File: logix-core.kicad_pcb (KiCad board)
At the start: 6 copper layers, 14 parts, among them U1 XC7A15T-FTG256

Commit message: stuff
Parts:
- added C14: 0.47u, Capacitor_SMD:C_0603_1608Metric, F.Cu at (237.7, 76.0)
- added C15: 10n, Capacitor_SMD:C_0603_1608Metric, F.Cu at (237.7, 78.5)
- added J1: QSH-030-01-X-D-A-XX, QSH-030-01-L-D-A-K:SAMTEC_QSH-030-01-X-D-A-XX, F.Cu at (222.2, 67.3)
- added J2: QSH-030-01-X-D-A-XX, QSH-030-01-L-D-A-K:SAMTEC_QSH-030-01-X-D-A-XX, F.Cu at (222.2, 79.5)
- added J3: 878321420, 878321420:CONN_87832-1420_MOL, F.Cu at (221.0, 91.3)
- added U2: MP5470GL-0000-P, MP5470:QFN-3x4_MP5470_MNP, F.Cu at (234.8, 90.1)
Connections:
- U1 pad F8: unconnected-(U1D-VCCBATT_0-PadF8) -> VCCAUX
- U1 pad G7: unconnected-(U1D-GNDADC_0-PadG7) -> AGND
- U1 pad G8: unconnected-(U1D-VCCADC_0-PadG8) -> VCCAUX
- U1 pad L7: unconnected-(U1C-TCK_0-PadL7) -> /FPGA/FPGA pg.3/JTAG.TCK
- U1 pad M7: unconnected-(U1C-TMS_0-PadM7) -> /FPGA/FPGA pg.3/JTAG.TMS
- U1 pad N7: unconnected-(U1C-TDI_0-PadN7) -> /FPGA/FPGA pg.3/JTAG.TDI
- U1 pad N8: unconnected-(U1C-TDO_0-PadN8) -> /FPGA/FPGA pg.3/JTAG.TDO
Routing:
- net VCCAUX: track 2.83 -> 4.24 mm, vias 4 -> 6
- net unconnected-(U1D-VCCBATT_0-PadF8): track 0.71 -> 0.00 mm, vias 1 -> 0
- net unconnected-(U1D-VCCADC_0-PadG8): track 0.71 -> 0.00 mm, vias 1 -> 0
- net unconnected-(U1D-GNDADC_0-PadG7): track 0.71 -> 0.00 mm, vias 1 -> 0
- net unconnected-(U1C-TMS_0-PadM7): track 0.71 -> 0.00 mm, vias 1 -> 0
- net unconnected-(U1C-TDO_0-PadN8): track 0.71 -> 0.00 mm, vias 1 -> 0
- net unconnected-(U1C-TDI_0-PadN7): track 0.71 -> 0.00 mm, vias 1 -> 0
- net unconnected-(U1C-TCK_0-PadL7): track 0.71 -> 0.00 mm, vias 1 -> 0
- net AGND: track 0.00 -> 0.71 mm, vias 0 -> 1
- net /FPGA/FPGA pg.3/JTAG.TMS: track 0.00 -> 0.71 mm, vias 0 -> 1
- net /FPGA/FPGA pg.3/JTAG.TDO: track 0.00 -> 0.71 mm, vias 0 -> 1
- net /FPGA/FPGA pg.3/JTAG.TDI: track 0.00 -> 0.71 mm, vias 0 -> 1
- net /FPGA/FPGA pg.3/JTAG.TCK: track 0.00 -> 0.71 mm, vias 0 -> 1

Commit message: more stuff!
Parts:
- added C16: 22u, Capacitor_SMD:C_0603_1608Metric, F.Cu at (188.0, 48.2)
- added C17: 22u, Capacitor_SMD:C_0603_1608Metric, F.Cu at (188.0, 50.7)
- added C18: 1u, Capacitor_SMD:C_0402_1005Metric, F.Cu at (187.4, 65.0)
- added C19: 22u, Capacitor_SMD:C_0603_1608Metric, F.Cu at (188.0, 53.2)
- added C20: 22u, Capacitor_SMD:C_0603_1608Metric, F.Cu at (188.0, 55.7)
- added C21: 22u, Capacitor_SMD:C_0603_1608Metric, F.Cu at (188.0, 58.2)
- added C22: 22u, Capacitor_SMD:C_0603_1608Metric, F.Cu at (188.0, 60.8)
- added C23: 47p, Capacitor_SMD:C_0402_1005Metric, F.Cu at (207.1, 90.8)
- added C24: 47p, Capacitor_SMD:C_0402_1005Metric, F.Cu at (207.1, 92.8)
- added C25: 10n, Capacitor_SMD:C_0402_1005Metric, F.Cu at (207.1, 94.7)
- added C26: 100n, Capacitor_SMD:C_0402_1005Metric, F.Cu at (207.1, 96.7)
- added C27: 100n, Capacitor_SMD:C_0402_1005Metric, F.Cu at (207.1, 98.7)
- added C28: 100n, Capacitor_SMD:C_0402_1005Metric, F.Cu at (207.1, 100.6)
- added D1: LED, LED_SMD:LED_0603_1608Metric, F.Cu at (207.7, 102.9)
- added D2: LED, LED_SMD:LED_0603_1608Metric, F.Cu at (207.7, 105.5)
- added FB1: FerriteBead, Resistor_SMD:R_0402_1005Metric_Pad0.72x0.64mm_HandSolder, F.Cu at (199.7, 97.8)
- added L1: 2.2u, Inductor_SMD:L_Bourns-SRN4018, F.Cu at (182.9, 49.7)
- added L2: 2.2u, Inductor_SMD:L_Bourns-SRN4018, F.Cu at (182.9, 55.3)
- added L3: 2.2u, Inductor_SMD:L_Bourns-SRN4018, F.Cu at (182.9, 60.8)
- added L4: 2.2u, Inductor_SMD:L_Bourns-SRN4018, F.Cu at (182.9, 66.4)
- added R1: 10k, Resistor_SMD:R_0402_1005Metric, F.Cu at (187.4, 63.0)
- added R10: 100, Resistor_SMD:R_0402_1005Metric_Pad0.72x0.64mm_HandSolder, F.Cu at (204.0, 106.7)
- added R2: 27.4, Resistor_SMD:R_0402_1005Metric_Pad0.72x0.64mm_HandSolder, F.Cu at (204.0, 90.8)
- added R3: 27.4, Resistor_SMD:R_0402_1005Metric_Pad0.72x0.64mm_HandSolder, F.Cu at (204.0, 92.8)
- added R4: 0, Resistor_SMD:R_0402_1005Metric_Pad0.72x0.64mm_HandSolder, F.Cu at (204.0, 94.8)
- added R5: 0, Resistor_SMD:R_0402_1005Metric_Pad0.72x0.64mm_HandSolder, F.Cu at (204.0, 96.8)
- added R6: 0, Resistor_SMD:R_0402_1005Metric_Pad0.72x0.64mm_HandSolder, F.Cu at (204.0, 98.8)
- added R7: 0, Resistor_SMD:R_0402_1005Metric_Pad0.72x0.64mm_HandSolder, F.Cu at (204.0, 100.7)
- added R8: 100, Resistor_SMD:R_0402_1005Metric_Pad0.72x0.64mm_HandSolder, F.Cu at (204.0, 102.7)
- added R9: 100, Resistor_SMD:R_0402_1005Metric_Pad0.72x0.64mm_HandSolder, F.Cu at (204.0, 104.7)
- added U3: TPUSBLC6-4SC6, Package_TO_SOT_SMD:SOT-23-6_Handsoldering, F.Cu at (195.1, 99.1)
- added U4: FT230XQ, Package_DFN_QFN:QFN-16-1EP_4x4mm_P0.65mm_EP2.1x2.1mm, F.Cu at (195.3, 93.6)
- added USB1: USB-MR-D-037, USB-MR-D-037:MICRO-USB-SMD_DEALON_USB-MR-D-037, F.Cu at (182.3, 93.2)
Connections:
- U2 pad 1: unconnected-(U2-VIN1-Pad1) -> /PMIC/VIN
- U2 pad 10: unconnected-(U2-FB3-Pad10) -> Net-(U2-FB3)
- U2 pad 13: unconnected-(U2-SW3-Pad13) -> Net-(U2-SW3)
- U2 pad 15: unconnected-(U2-SW4-Pad15) -> Net-(U2-SW4)
- U2 pad 16: unconnected-(U2-VCC-Pad16) -> Net-(U2-VCC)
- U2 pad 18: unconnected-(U2-FB4-Pad18) -> Net-(U2-FB4)
- U2 pad 2: unconnected-(U2-SW1-Pad2) -> Net-(U2-SW1)
- U2 pad 20: unconnected-(U2-GPIO-Pad20) -> Net-(U2-GPIO)
- U2 pad 21: unconnected-(U2-SGND1-Pad21) -> GND
- U2 pad 22: unconnected-(U2-FB1-Pad22) -> Net-(U2-FB1)
- U2 pad 4: unconnected-(U2-SW2-Pad4) -> Net-(U2-SW2)
- U2 pad 5: unconnected-(U2-VIN2-Pad5) -> /PMIC/VIN
- U2 pad 6: unconnected-(U2-FB2-Pad6) -> Net-(U2-FB2)
- U2 pad 9: unconnected-(U2-SGND2-Pad9) -> GND

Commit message: more stuff
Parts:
- added U5: MX25L3233FZN, Package_SON:WSON-8-1EP_6x5mm_P1.27mm_EP3.4x4mm, F.Cu at (202.3, 61.1)

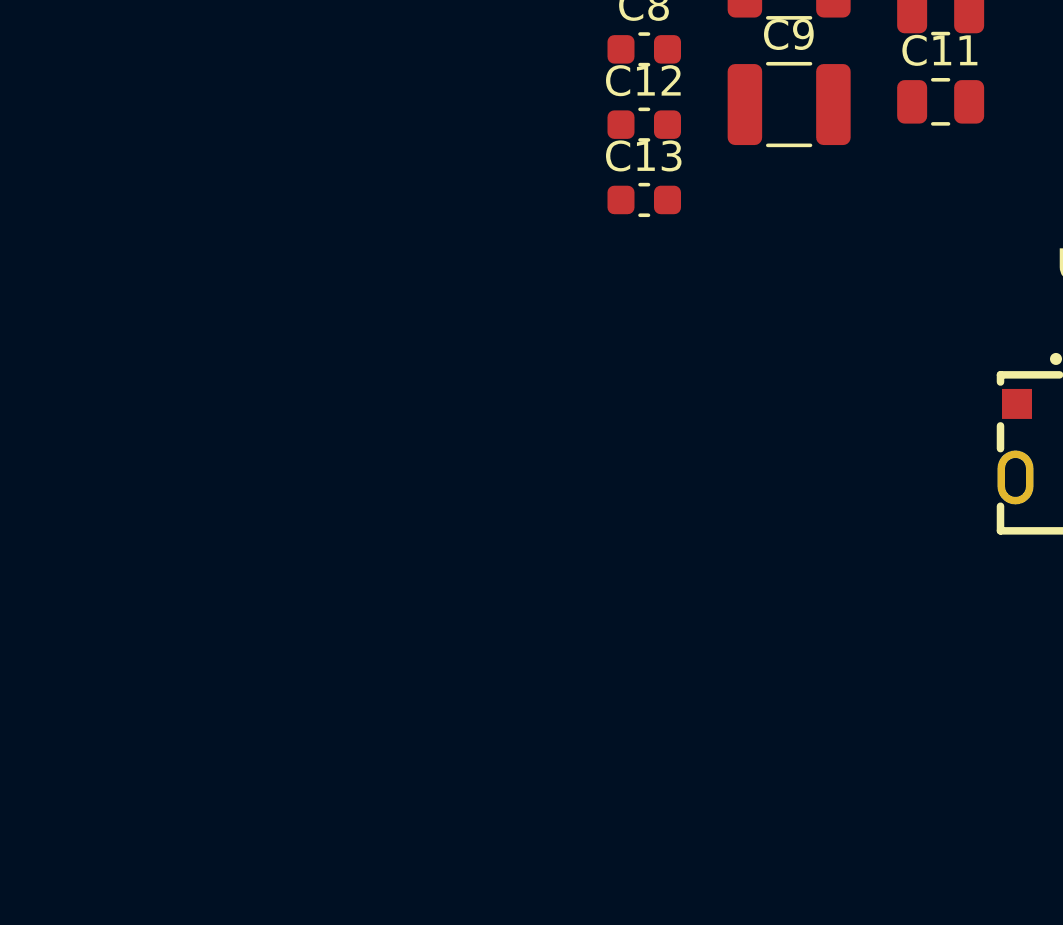
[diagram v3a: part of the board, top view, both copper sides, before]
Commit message: changed ftg256 to csg325, wanted xc7a12t but couldnt find
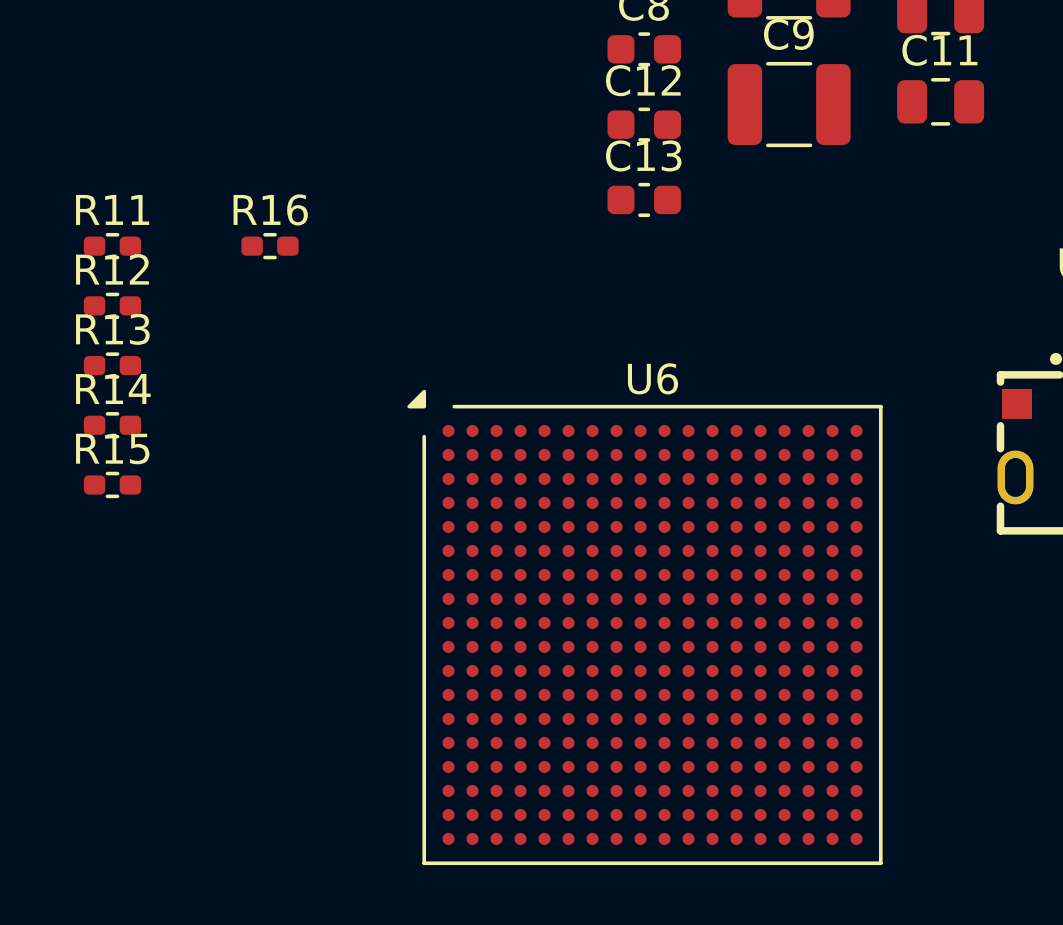
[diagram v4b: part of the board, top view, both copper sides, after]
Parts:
- added R11: 0, Resistor_SMD:R_0402_1005Metric_Pad0.72x0.64mm_HandSolder, F.Cu at (149.0, 87.0)
- added R12: 0, Resistor_SMD:R_0402_1005Metric_Pad0.72x0.64mm_HandSolder, F.Cu at (149.0, 89.0)
- added R13: 0, Resistor_SMD:R_0402_1005Metric_Pad0.72x0.64mm_HandSolder, F.Cu at (149.0, 91.0)
- added R14: 0, Resistor_SMD:R_0402_1005Metric_Pad0.72x0.64mm_HandSolder, F.Cu at (149.0, 93.0)
- added R15: 0, Resistor_SMD:R_0402_1005Metric_Pad0.72x0.64mm_HandSolder, F.Cu at (149.0, 95.0)
- added R16: 0, Resistor_SMD:R_0402_1005Metric_Pad0.72x0.64mm_HandSolder, F.Cu at (154.2, 87.0)
- added U6: XC7A15T-CSG325, Package_BGA:Xilinx_CSG325, F.Cu at (167.0, 100.0)
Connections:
- U1 pad A1: GND -> (no net)
- U1 pad A11: GND -> (no net)
- U1 pad A2: unconnected-(U1B-IO_L8N_T1_AD14N_35-PadA2) -> (no net)
- U1 pad A3: unconnected-(U1B-IO_L4N_T0_35-PadA3) -> (no net)
- U1 pad A4: unconnected-(U1B-IO_L3N_T0_DQS_AD5N_35-PadA4) -> (no net)
- U1 pad A5: unconnected-(U1B-IO_L3P_T0_DQS_AD5P_35-PadA5) -> (no net)
- U1 pad A6: unconnected-(U1B-VCCO_35-PadA6) -> (no net)
- U1 pad A7: unconnected-(U1B-IO_L1N_T0_AD4N_35-PadA7) -> (no net)
- U1 pad B1: unconnected-(U1B-IO_L9N_T1_DQS_AD7N_35-PadB1) -> (no net)
- U1 pad B2: unconnected-(U1B-IO_L8P_T1_AD14P_35-PadB2) -> (no net)
- U1 pad B3: unconnected-(U1B-VCCO_35-PadB3) -> (no net)
- U1 pad B4: unconnected-(U1B-IO_L4P_T0_35-PadB4) -> (no net)
- U1 pad B5: unconnected-(U1B-IO_L2N_T0_AD12N_35-PadB5) -> (no net)
- U1 pad B6: unconnected-(U1B-IO_L2P_T0_AD12P_35-PadB6) -> (no net)
- U1 pad B7: unconnected-(U1B-IO_L1P_T0_AD4P_35-PadB7) -> (no net)
- U1 pad B8: GND -> (no net)
- U1 pad C1: unconnected-(U1B-IO_L9P_T1_DQS_AD7P_35-PadC1) -> (no net)
- U1 pad C15: GND -> (no net)
- U1 pad C2: unconnected-(U1B-IO_L7N_T1_AD6N_35-PadC2) -> (no net)
- U1 pad C3: unconnected-(U1B-IO_L7P_T1_AD6P_35-PadC3) -> (no net)
- U1 pad C4: unconnected-(U1B-IO_L12N_T1_MRCC_35-PadC4) -> (no net)
- U1 pad C5: GND -> (no net)
- U1 pad C6: unconnected-(U1B-IO_L5N_T0_AD13N_35-PadC6) -> (no net)
- U1 pad C7: unconnected-(U1B-IO_L5P_T0_AD13P_35-PadC7) -> (no net)
- U1 pad D1: unconnected-(U1B-IO_L10N_T1_AD15N_35-PadD1) -> (no net)
- U1 pad D12: GND -> (no net)
- U1 pad D2: GND -> (no net)
- U1 pad D3: unconnected-(U1B-IO_L11N_T1_SRCC_35-PadD3) -> (no net)
- U1 pad D4: unconnected-(U1B-IO_L12P_T1_MRCC_35-PadD4) -> (no net)
- U1 pad D5: unconnected-(U1B-IO_L6N_T0_VREF_35-PadD5) -> (no net)
- U1 pad D6: unconnected-(U1B-IO_L6P_T0_35-PadD6) -> (no net)
- U1 pad D7: unconnected-(U1B-VCCO_35-PadD7) -> (no net)
- U1 pad E1: unconnected-(U1B-IO_L15N_T2_DQS_35-PadE1) -> (no net)
- U1 pad E10: VCCBRAM -> (no net)
- U1 pad E2: unconnected-(U1B-IO_L10P_T1_AD15P_35-PadE2) -> (no net)
- U1 pad E3: unconnected-(U1B-IO_L11P_T1_SRCC_35-PadE3) -> (no net)
- U1 pad E4: unconnected-(U1B-VCCO_35-PadE4) -> (no net)
- U1 pad E5: unconnected-(U1B-IO_L13N_T2_MRCC_35-PadE5) -> (no net)
- U1 pad E6: unconnected-(U1B-IO_0_35-PadE6) -> (no net)
- U1 pad E8: unconnected-(U1C-CCLK_0-PadE8) -> /FPGA/FPGA pg.3/INT_FLASH_SPI_CLK
- U1 pad E9: GND -> (no net)
- U1 pad F1: unconnected-(U1B-VCCO_35-PadF1) -> (no net)
- U1 pad F10: GND -> (no net)
- U1 pad F11: VCCBRAM -> (no net)
- U1 pad F16: GND -> (no net)
- U1 pad F2: unconnected-(U1B-IO_L15P_T2_DQS_35-PadF2) -> (no net)
- U1 pad F3: unconnected-(U1B-IO_L14N_T2_SRCC_35-PadF3) -> (no net)
- U1 pad F4: unconnected-(U1B-IO_L14P_T2_SRCC_35-PadF4) -> (no net)
- U1 pad F5: unconnected-(U1B-IO_L13P_T2_MRCC_35-PadF5) -> (no net)
- U1 pad F6: GND -> (no net)
- U1 pad F7: VCCINT -> (no net)
- U1 pad F8: VCCAUX -> (no net)
- U1 pad F9: VCCINT -> (no net)
- U1 pad G1: unconnected-(U1B-IO_L17N_T2_35-PadG1) -> (no net)
- U1 pad G10: VCCAUX -> (no net)
- U1 pad G13: GND -> (no net)
- U1 pad G2: unconnected-(U1B-IO_L17P_T2_35-PadG2) -> (no net)
- U1 pad G3: GND -> (no net)
- U1 pad G4: unconnected-(U1B-IO_L16N_T2_35-PadG4) -> (no net)
- U1 pad G5: unconnected-(U1B-IO_L16P_T2_35-PadG5) -> (no net)
- U1 pad G6: VCCINT -> (no net)
- U1 pad G7: AGND -> (no net)
- U1 pad G8: VCCAUX -> (no net)
- U1 pad G9: GND -> (no net)
- U1 pad H1: unconnected-(U1B-IO_L20N_T3_35-PadH1) -> (no net)
- U1 pad H2: unconnected-(U1B-IO_L20P_T3_35-PadH2) -> (no net)
- U1 pad H3: unconnected-(U1B-IO_L21N_T3_DQS_35-PadH3) -> (no net)
- U1 pad H4: unconnected-(U1B-IO_L18N_T2_35-PadH4) -> (no net)
- U1 pad H5: unconnected-(U1B-IO_L18P_T2_35-PadH5) -> (no net)
- U1 pad H6: GND -> (no net)
- U1 pad H9: VCCINT -> (no net)
- U1 pad J1: unconnected-(U1B-IO_L22N_T3_35-PadJ1) -> (no net)
- U1 pad J10: VCCAUX -> (no net)
- U1 pad J11: GND -> (no net)
- U1 pad J13: unconnected-(U1A-IO_L1P_T0_D00_MOSI_14-PadJ13) -> /FPGA/FPGA pg.1/INT_FLASH_SPI_D0
- U1 pad J14: unconnected-(U1A-IO_L1N_T0_D01_DIN_14-PadJ14) -> /FPGA/FPGA pg.1/INT_FLASH_SPI_D1
- U1 pad J2: unconnected-(U1B-VCCO_35-PadJ2) -> (no net)
- U1 pad J3: unconnected-(U1B-IO_L21P_T3_DQS_35-PadJ3) -> (no net)
- U1 pad J4: unconnected-(U1B-IO_L19N_T3_VREF_35-PadJ4) -> (no net)
- U1 pad J5: unconnected-(U1B-IO_L19P_T3_35-PadJ5) -> (no net)
- U1 pad J6: VCCINT -> (no net)
- U1 pad J9: GND -> (no net)
- U1 pad K1: unconnected-(U1B-IO_L22P_T3_35-PadK1) -> (no net)
- U1 pad K11: VCCAUX -> (no net)
- U1 pad K14: GND -> (no net)
- U1 pad K15: unconnected-(U1A-IO_L2P_T0_D02_14-PadK15) -> /FPGA/FPGA pg.1/INT_FLASH_SPI_D2
- U1 pad K16: unconnected-(U1A-IO_L2N_T0_D03_14-PadK16) -> /FPGA/FPGA pg.1/INT_FLASH_SPI_D3
- U1 pad K2: unconnected-(U1B-IO_L24N_T3_35-PadK2) -> (no net)
- U1 pad K3: unconnected-(U1B-IO_L24P_T3_35-PadK3) -> (no net)
- U1 pad K4: GND -> (no net)
- U1 pad K5: unconnected-(U1B-IO_25_35-PadK5) -> (no net)
- U1 pad K6: GND -> (no net)
- U1 pad K9: VCCINT -> (no net)
- U1 pad L1: GND -> (no net)
- U1 pad L10: VCCAUX -> (no net)
- U1 pad L11: GND -> (no net)
- U1 pad L12: unconnected-(U1A-IO_L6P_T0_FCS_B_14-PadL12) -> /FPGA/FPGA pg.1/INT_FLASH_SPI_CS#
- U1 pad L2: unconnected-(U1B-IO_L23N_T3_35-PadL2) -> (no net)
- U1 pad L3: unconnected-(U1B-IO_L23P_T3_35-PadL3) -> (no net)
- U1 pad L4: unconnected-(U1B-IO_L1P_T0_34-PadL4) -> (no net)
- U1 pad L5: unconnected-(U1B-IO_0_34-PadL5) -> (no net)
- U1 pad L8: VCCINT -> (no net)
- U1 pad M1: unconnected-(U1B-IO_L2N_T0_34-PadM1) -> (no net)
- U1 pad M2: unconnected-(U1B-IO_L2P_T0_34-PadM2) -> (no net)
- U1 pad M3: unconnected-(U1B-VCCO_34-PadM3) -> (no net)
- U1 pad M4: unconnected-(U1B-IO_L1N_T0_34-PadM4) -> (no net)
- U1 pad M5: unconnected-(U1B-IO_L6P_T0_34-PadM5) -> (no net)
- U1 pad M8: GND -> (no net)
- U1 pad N1: unconnected-(U1B-IO_L4P_T0_34-PadN1) -> (no net)
- U1 pad N15: GND -> (no net)
- U1 pad N2: unconnected-(U1B-IO_L3N_T0_DQS_34-PadN2) -> (no net)
- U1 pad N3: unconnected-(U1B-IO_L3P_T0_DQS_34-PadN3) -> (no net)
- U1 pad N4: unconnected-(U1B-IO_L6N_T0_VREF_34-PadN4) -> (no net)
- U1 pad N5: GND -> (no net)
- U1 pad P1: unconnected-(U1B-IO_L4N_T0_34-PadP1) -> (no net)
- U1 pad P12: GND -> (no net)
- U1 pad P2: GND -> (no net)
- U1 pad P3: unconnected-(U1B-IO_L5N_T0_34-PadP3) -> (no net)
- U1 pad P4: unconnected-(U1B-IO_L5P_T0_34-PadP4) -> (no net)
- U1 pad P5: unconnected-(U1B-IO_L10P_T1_34-PadP5) -> (no net)
- U1 pad R1: unconnected-(U1B-IO_L7N_T1_34-PadR1) -> (no net)
- U1 pad R2: unconnected-(U1B-IO_L7P_T1_34-PadR2) -> (no net)
- U1 pad R3: unconnected-(U1B-IO_L8P_T1_34-PadR3) -> (no net)
- U1 pad R4: unconnected-(U1B-VCCO_34-PadR4) -> (no net)
- U1 pad R9: GND -> (no net)
- U1 pad T1: unconnected-(U1B-VCCO_34-PadT1) -> (no net)
- U1 pad T16: GND -> (no net)
- U1 pad T2: unconnected-(U1B-IO_L8N_T1_34-PadT2) -> (no net)
- U1 pad T3: unconnected-(U1B-IO_L9N_T1_DQS_34-PadT3) -> (no net)
- U1 pad T4: unconnected-(U1B-IO_L9P_T1_DQS_34-PadT4) -> (no net)
- U1 pad T6: GND -> (no net)
- U5 pad 1: unconnected-(U5-~{CS}-Pad1) -> /SPI Flash/FLASH_SPI.CS#
- U5 pad 2: unconnected-(U5-SO/SIO1-Pad2) -> /SPI Flash/FLASH_SPI.D1
- U5 pad 3: unconnected-(U5-~{WP}/SIO2-Pad3) -> /SPI Flash/FLASH_SPI.D2
- U5 pad 4: unconnected-(U5-GND-Pad4) -> GND
- U5 pad 5: unconnected-(U5-SI/SIO0-Pad5) -> /SPI Flash/FLASH_SPI.D0
- U5 pad 6: unconnected-(U5-SCLK-Pad6) -> /SPI Flash/FLASH_SPI.CLK
- U5 pad 7: unconnected-(U5-~{HOLD}/SIO3-Pad7) -> /SPI Flash/FLASH_SPI.D3
- U5 pad 8: unconnected-(U5-VCC-Pad8) -> Net-(U5-VCC)
- U5 pad 9: unconnected-(U5-EP-Pad9) -> GND
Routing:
- net (no net): track 0.00 -> 55.9 mm, vias 0 -> 79
- net unconnected-(U1C-CCLK_0-PadE8): track 0.71 -> 0.00 mm, vias 1 -> 0
- net unconnected-(U1B-VCCO_35-PadJ2): track 0.71 -> 0.00 mm, vias 1 -> 0
- net unconnected-(U1B-VCCO_35-PadF1): track 0.71 -> 0.00 mm, vias 1 -> 0
- net unconnected-(U1B-VCCO_35-PadE4): track 0.71 -> 0.00 mm, vias 1 -> 0
- net unconnected-(U1B-VCCO_35-PadD7): track 0.71 -> 0.00 mm, vias 1 -> 0
- net unconnected-(U1B-VCCO_35-PadB3): track 0.71 -> 0.00 mm, vias 1 -> 0
- net unconnected-(U1B-VCCO_35-PadA6): track 0.71 -> 0.00 mm, vias 1 -> 0
- net unconnected-(U1B-VCCO_34-PadT1): track 0.71 -> 0.00 mm, vias 1 -> 0
- net unconnected-(U1B-VCCO_34-PadR4): track 0.71 -> 0.00 mm, vias 1 -> 0
- net unconnected-(U1B-VCCO_34-PadM3): track 0.71 -> 0.00 mm, vias 1 -> 0
- net unconnected-(U1B-IO_L9P_T1_DQS_AD7P_35-PadC1): track 0.71 -> 0.00 mm, vias 1 -> 0
- net unconnected-(U1B-IO_L9P_T1_DQS_34-PadT4): track 0.71 -> 0.00 mm, vias 1 -> 0
- net unconnected-(U1B-IO_L9N_T1_DQS_AD7N_35-PadB1): track 0.71 -> 0.00 mm, vias 1 -> 0
- net unconnected-(U1B-IO_L9N_T1_DQS_34-PadT3): track 0.71 -> 0.00 mm, vias 1 -> 0
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
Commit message: stuff
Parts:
- added R17: R, Resistor_SMD:R_0402_1005Metric_Pad0.72x0.64mm_HandSolder, F.Cu at (152.0, 106.0)
- moved J1 78.4 mm to (167.2, 123.2)
- moved J2 27.0 mm to (230.5, 105.2)
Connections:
- net Net-(U2-FB2) renamed +3.3V
- net Net-(U2-FB3) renamed +1V8
- net Net-(U2-FB4) renamed +1V5
- C16 pad 1: /PMIC/VIN -> VBUS
- C17 pad 1: /PMIC/VIN -> VBUS
- C19 pad 1: Net-(U2-FB1) -> VCCINT
- J1 pad 01: unconnected-(J1-Pad01) -> /DI.DI2+
- J1 pad 02: unconnected-(J1-Pad02) -> /DI.DI1+
- J1 pad 03: unconnected-(J1-Pad03) -> /DI.DI2-
- J1 pad 04: unconnected-(J1-Pad04) -> /DI.DI1-
- J1 pad 05: unconnected-(J1-Pad05) -> /DI.DI3+
- J1 pad 06: unconnected-(J1-Pad06) -> /DO.DO1+
- J1 pad 07: unconnected-(J1-Pad07) -> /DI.DI3-
- J1 pad 08: unconnected-(J1-Pad08) -> /DO.DO1-
- J1 pad 09: unconnected-(J1-Pad09) -> /DI.DI4+
- J1 pad 10: unconnected-(J1-Pad10) -> /DO.DO2+
- J1 pad 11: unconnected-(J1-Pad11) -> /DI.DI4-
- J1 pad 12: unconnected-(J1-Pad12) -> /DO.DO2-
- J1 pad 13: unconnected-(J1-Pad13) -> /DI.DI5+
- J1 pad 14: unconnected-(J1-Pad14) -> /DO.DO3+
- J1 pad 15: unconnected-(J1-Pad15) -> /DI.DI5-
- J1 pad 16: unconnected-(J1-Pad16) -> /DO.DO3-
- J1 pad 17: unconnected-(J1-Pad17) -> /DI.DI6+
- J1 pad 18: unconnected-(J1-Pad18) -> /DO.DO4+
- J1 pad 19: unconnected-(J1-Pad19) -> /DI.DI6-
- J1 pad 20: unconnected-(J1-Pad20) -> /DO.DO4-
- J1 pad 21: unconnected-(J1-Pad21) -> /DI.DI7+
- J1 pad 22: unconnected-(J1-Pad22) -> /DO.DO5+
- J1 pad 23: unconnected-(J1-Pad23) -> /DI.DI7-
- J1 pad 24: unconnected-(J1-Pad24) -> /DO.DO5-
- J1 pad 25: unconnected-(J1-Pad25) -> /DI.DI8+
- J1 pad 26: unconnected-(J1-Pad26) -> /DO.DO6+
- J1 pad 27: unconnected-(J1-Pad27) -> /DI.DI8-
- J1 pad 28: unconnected-(J1-Pad28) -> /DO.DO6-
- J1 pad 29: unconnected-(J1-Pad29) -> /DI.DI9+
- J1 pad 30: unconnected-(J1-Pad30) -> /DO.DO7+
- J1 pad 31: unconnected-(J1-Pad31) -> /DI.DI9-
- J1 pad 32: unconnected-(J1-Pad32) -> /DO.DO7-
- J1 pad 33: unconnected-(J1-Pad33) -> /DI.DI10+
- J1 pad 34: unconnected-(J1-Pad34) -> /DO.DO8+
- J1 pad 35: unconnected-(J1-Pad35) -> /DI.DI10-
- J1 pad 36: unconnected-(J1-Pad36) -> /DO.DO8-
- J1 pad 37: unconnected-(J1-Pad37) -> /DI.DI11+
- J1 pad 39: unconnected-(J1-Pad39) -> /DI.DI11-
- J1 pad 41: unconnected-(J1-Pad41) -> /DI.DI12+
- J1 pad 43: unconnected-(J1-Pad43) -> /DI.DI12-
- J1 pad 45: unconnected-(J1-Pad45) -> /DI.DI13+
- J1 pad 47: unconnected-(J1-Pad47) -> /DI.DI13-
- J1 pad 49: unconnected-(J1-Pad49) -> /DI.DI14+
- J1 pad 51: unconnected-(J1-Pad51) -> /DI.DI14-
- J1 pad 53: unconnected-(J1-Pad53) -> /DI.DI15+
- J1 pad 55: unconnected-(J1-Pad55) -> /DI.DI15-
- J1 pad 57: unconnected-(J1-Pad57) -> /DI.DI16+
- J1 pad 59: unconnected-(J1-Pad59) -> /DI.DI16-
- L1 pad 2: Net-(U2-FB1) -> VCCINT
- U2 pad 1: /PMIC/VIN -> VBUS
- U2 pad 12: unconnected-(U2-EN/SYNC-Pad12) -> /PMIC/EN
- U2 pad 14: unconnected-(U2-GND-Pad14) -> GND
- U2 pad 19: unconnected-(U2-AGND-Pad19) -> GND
- U2 pad 22: Net-(U2-FB1) -> VCCINT
- U2 pad 3: unconnected-(U2-GND-Pad3) -> GND
- U2 pad 5: /PMIC/VIN -> VBUS
- U2 pad 7: unconnected-(U2-SCL-Pad7) -> /PMIC/I2C.SCL
- U2 pad 8: unconnected-(U2-SDA-Pad8) -> /PMIC/I2C.SDA
- U6 pad A10: unconnected-(U6A-IO_L5N_T0_AD9N_15-PadA10) -> /DI.DI5-
- U6 pad A12: unconnected-(U6A-IO_L7N_T1_AD2N_15-PadA12) -> /DI.DI7-
- U6 pad A13: unconnected-(U6A-IO_L8P_T1_AD10P_15-PadA13) -> /DI.DI8+
- U6 pad A14: unconnected-(U6A-IO_L8N_T1_AD10N_15-PadA14) -> /DI.DI8-
- U6 pad A15: unconnected-(U6A-IO_L10N_T1_AD11N_15-PadA15) -> /DI.DI10-
- U6 pad A17: unconnected-(U6A-IO_L15N_T2_DQS_ADV_B_15-PadA17) -> /DI.DI15-
- U6 pad A3: unconnected-(U6C-MGTPRXN1_216-PadA3) -> /FPGA/FPGA pg.3/GTP1_RX-
- U6 pad A4: unconnected-(U6C-MGTPRXP1_216-PadA4) -> /FPGA/FPGA pg.3/GTP1_RX+
- U6 pad A9: unconnected-(U6A-IO_L3N_T0_DQS_AD1N_15-PadA9) -> /DI.DI3-
- U6 pad B1: unconnected-(U6C-MGTPTXN3_216-PadB1) -> /FPGA/FPGA pg.3/GTP3_TX-
- U6 pad B10: unconnected-(U6A-IO_L5P_T0_AD9P_15-PadB10) -> /DI.DI5+
- U6 pad B11: unconnected-(U6A-IO_L4N_T0_15-PadB11) -> /DI.DI4-
- U6 pad B12: unconnected-(U6A-IO_L7P_T1_AD2P_15-PadB12) -> /DI.DI7+
- U6 pad B14: unconnected-(U6A-IO_L10P_T1_AD11P_15-PadB14) -> /DI.DI10+
- U6 pad B15: unconnected-(U6A-IO_L9N_T1_DQS_AD3N_15-PadB15) -> /DI.DI9-
- U6 pad B16: unconnected-(U6A-IO_L15P_T2_DQS_15-PadB16) -> /DI.DI15+
- U6 pad B17: unconnected-(U6A-IO_L16N_T2_A27_15-PadB17) -> /DI.DI16-
- U6 pad B2: unconnected-(U6C-MGTPTXP3_216-PadB2) -> /FPGA/FPGA pg.3/GTP3_TX+
- U6 pad B5: unconnected-(U6C-MGTREFCLK1N_216-PadB5) -> /FPGA/FPGA pg.3/GT_REFCLK1+
- U6 pad B6: unconnected-(U6C-MGTREFCLK1P_216-PadB6) -> /FPGA/FPGA pg.3/GT_REFCLK1+
- U6 pad B9: unconnected-(U6A-IO_L3P_T0_DQS_AD1P_15-PadB9) -> /DI.DI3+
- U6 pad C11: unconnected-(U6A-IO_L4P_T0_15-PadC11) -> /DI.DI4+
- U6 pad C12: unconnected-(U6A-IO_L6N_T0_VREF_15-PadC12) -> /DI.DI6-
- U6 pad C13: unconnected-(U6A-IO_L11N_T1_SRCC_15-PadC13) -> /DI.DI11-
- U6 pad C14: unconnected-(U6A-IO_L9P_T1_DQS_AD3P_15-PadC14) -> /DI.DI9+
- U6 pad C16: unconnected-(U6A-IO_L16P_T2_A28_15-PadC16) -> /DI.DI16+
- U6 pad C3: unconnected-(U6C-MGTPRXN2_216-PadC3) -> /FPGA/FPGA pg.3/GTP2_RX-
- U6 pad C4: unconnected-(U6C-MGTPRXP2_216-PadC4) -> /FPGA/FPGA pg.3/GTP2_RX+
- U6 pad C8: unconnected-(U6A-IO_L1N_T0_AD0N_15-PadC8) -> /DI.DI1-
- U6 pad C9: unconnected-(U6A-IO_L2N_T0_AD8N_15-PadC9) -> /DI.DI2-
- U6 pad D1: unconnected-(U6C-MGTPTXN2_216-PadD1) -> /FPGA/FPGA pg.3/GTP2_TX-
- U6 pad D11: unconnected-(U6A-IO_L6P_T0_15-PadD11) -> /DI.DI6+
- U6 pad D13: unconnected-(U6A-IO_L11P_T1_SRCC_15-PadD13) -> /DI.DI11+
- U6 pad D14: unconnected-(U6A-IO_L12N_T1_MRCC_15-PadD14) -> /DI.DI12-
- U6 pad D15: unconnected-(U6A-IO_L13N_T2_MRCC_15-PadD15) -> /DI.DI13-
- U6 pad D16: unconnected-(U6A-IO_L14N_T2_SRCC_15-PadD16) -> /DI.DI14-
- U6 pad D2: unconnected-(U6C-MGTPTXP2_216-PadD2) -> /FPGA/FPGA pg.3/GTP2_TX+
- U6 pad D5: unconnected-(U6C-MGTREFCLK0N_216-PadD5) -> /FPGA/FPGA pg.3/GT_REFCLK0-
- U6 pad D6: unconnected-(U6C-MGTREFCLK0P_216-PadD6) -> /FPGA/FPGA pg.3/GT_REFCLK0+
- U6 pad D8: unconnected-(U6A-IO_L1P_T0_AD0P_15-PadD8) -> /DI.DI1+
- U6 pad D9: unconnected-(U6A-IO_L2P_T0_AD8P_15-PadD9) -> /DI.DI2+
- U6 pad E13: unconnected-(U6A-IO_L12P_T1_MRCC_15-PadE13) -> /DI.DI12+
- U6 pad E15: unconnected-(U6A-IO_L13P_T2_MRCC_15-PadE15) -> /DI.DI13+
- U6 pad E16: unconnected-(U6A-IO_L14P_T2_SRCC_15-PadE16) -> /DI.DI14+
- U6 pad E3: unconnected-(U6C-MGTPRXN0_216-PadE3) -> /FPGA/FPGA pg.3/GTP0_RX-
- U6 pad E4: unconnected-(U6C-MGTPRXP0_216-PadE4) -> /FPGA/FPGA pg.3/GTP0_RX+
- U6 pad F1: unconnected-(U6C-MGTPTXN1_216-PadF1) -> /FPGA/FPGA pg.3/GTP1_TX-
- U6 pad F2: unconnected-(U6C-MGTPTXP1_216-PadF2) -> /FPGA/FPGA pg.3/GTP1_TX+
- U6 pad G3: unconnected-(U6C-MGTPRXN3_216-PadG3) -> /FPGA/FPGA pg.3/GTP3_RX-
- U6 pad G4: unconnected-(U6C-MGTPRXP3_216-PadG4) -> /FPGA/FPGA pg.3/GTP3_RX+
- U6 pad H1: unconnected-(U6C-MGTPTXN0_216-PadH1) -> /FPGA/FPGA pg.3/GTP0_TX-
- U6 pad H2: unconnected-(U6C-MGTPTXP0_216-PadH2) -> /FPGA/FPGA pg.3/GTP0_TX+
- U6 pad J14: unconnected-(U6A-IO_L5P_T0_D06_14-PadJ14) -> /DO.DO3+
- U6 pad J18: unconnected-(U6A-IO_L3P_T0_DQS_PUDC_B_14-PadJ18) -> /DO.DO1+
- U6 pad K15: unconnected-(U6A-IO_L5N_T0_D07_14-PadK15) -> /DO.DO3-
- U6 pad K17: unconnected-(U6A-IO_L4P_T0_D04_14-PadK17) -> /DO.DO2+
- U6 pad K18: unconnected-(U6A-IO_L3N_T0_DQS_EMCCLK_14-PadK18) -> /DO.DO1-
- U6 pad L18: unconnected-(U6A-IO_L4N_T0_D05_14-PadL18) -> /DO.DO2-
- U6 pad M14: unconnected-(U6A-IO_L8P_T1_D11_14-PadM14) -> /DO.DO5+
- U6 pad M16: unconnected-(U6A-IO_L7P_T1_D09_14-PadM16) -> /DO.DO4+
- U6 pad M17: unconnected-(U6A-IO_L7N_T1_D10_14-PadM17) -> /DO.DO4-
- U6 pad N14: unconnected-(U6A-IO_L8N_T1_D12_14-PadN14) -> /DO.DO5-
- U6 pad N16: unconnected-(U6A-IO_L9P_T1_DQS_14-PadN16) -> /DO.DO6+
- U6 pad N17: unconnected-(U6A-IO_L9N_T1_DQS_D13_14-PadN17) -> /DO.DO6-
- U6 pad N18: unconnected-(U6A-IO_L10P_T1_D14_14-PadN18) -> /DO.DO7+
- U6 pad P15: unconnected-(U6A-IO_L11P_T1_SRCC_14-PadP15) -> /DO.DO8+
- U6 pad P16: unconnected-(U6A-IO_L11N_T1_SRCC_14-PadP16) -> /DO.DO8-
- U6 pad P18: unconnected-(U6A-IO_L10N_T1_D15_14-PadP18) -> /DO.DO7-
